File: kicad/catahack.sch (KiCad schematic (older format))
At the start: 0 parts

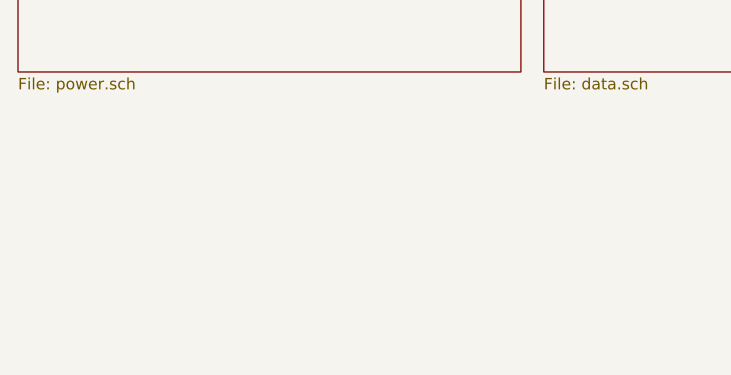
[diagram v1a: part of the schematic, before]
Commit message: Initial footprint placement + changes
* Added initial placement
* Remove pull-down resistors from USB lines.
* Remove ferrite bead from FTDI chip as it was very close to Vcc FB
* Fixed MAX TX pins
* Assigned footprints.
* Removed redundant solder jumpers.
* Small changes for layout coherence.
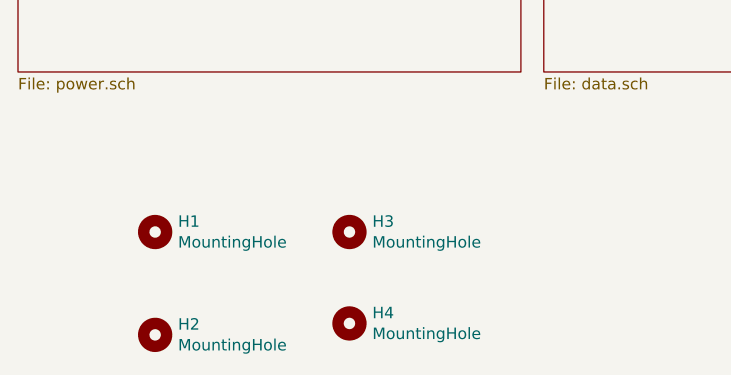
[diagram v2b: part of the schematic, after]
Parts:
- added H1, H2, H3, H4: MountingHole, MountingHole:MountingHole_4.3mm_M4_ISO7380_Pad, symbol Mechanical:MountingHole
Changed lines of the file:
@@
 F1 "audio.sch" 50
 $EndSheet
+$Comp
+L Mechanical:MountingHole H1
+U 1 1 5FBD6C90
+P 1900 3400
+F 0 "H1" H 2000 3446 50  0000 L CNN
+F 1 "MountingHole" H 2000 3355 50  0000 L CNN
+F 2 "MountingHole:MountingHole_4.3mm_M4_ISO7380_Pad" H 1900 3400 50  0001 C CNN
+F 3 "~" H 1900 3400 50  0001 C CNN
+	1    1900 3400
+	1    0    0    -1
+$EndComp
+$Comp
+L Mechanical:MountingHole H3
+U 1 1 5FBD75AF
+P 2750 3400
+F 0 "H3" H 2850 3446 50  0000 L CNN
+F 1 "MountingHole" H 2850 3355 50  0000 L CNN
+F 2 "MountingHole:MountingHole_4.3mm_M4_ISO7380_Pad" H 2750 3400 50  0001 C CNN
+F 3 "~" H 2750 3400 50  0001 C CNN
+	1    2750 3400
+	1    0    0    -1
+$EndComp
+$Comp
+L Mechanical:MountingHole H2
+U 1 1 5FBD795B
+P 1900 3850
+F 0 "H2" H 2000 3896 50  0000 L CNN
+F 1 "MountingHole" H 2000 3805 50  0000 L CNN
+F 2 "MountingHole:MountingHole_4.3mm_M4_ISO7380_Pad" H 1900 3850 50  0001 C CNN
+F 3 "~" H 1900 3850 50  0001 C CNN
+	1    1900 3850
+	1    0    0    -1
+$EndComp
+$Comp
+L Mechanical:MountingHole H4
+U 1 1 5FBD81A5
+P 2750 3800
+F 0 "H4" H 2850 3846 50  0000 L CNN
+F 1 "MountingHole" H 2850 3755 50  0000 L CNN
+F 2 "MountingHole:MountingHole_4.3mm_M4_ISO7380_Pad" H 2750 3800 50  0001 C CNN
+F 3 "~" H 2750 3800 50  0001 C CNN
+	1    2750 3800
+	1    0    0    -1
+$EndComp
 $EndSCHEMATC
